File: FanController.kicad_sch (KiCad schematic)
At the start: 28 parts, among them J1 Conn_01x02_Female, J2 Conn_01x03_Male, J3 Conn_01x03_Male, J4 Conn_01x03_Male, J5 Conn_01x03_Male, Q1 AO3400A, Q2 AO3400A, Q3 AO3400A, Q4 AO3400A, U1 D-SUN-MP1584EN, U2 mh-et-live-minikit

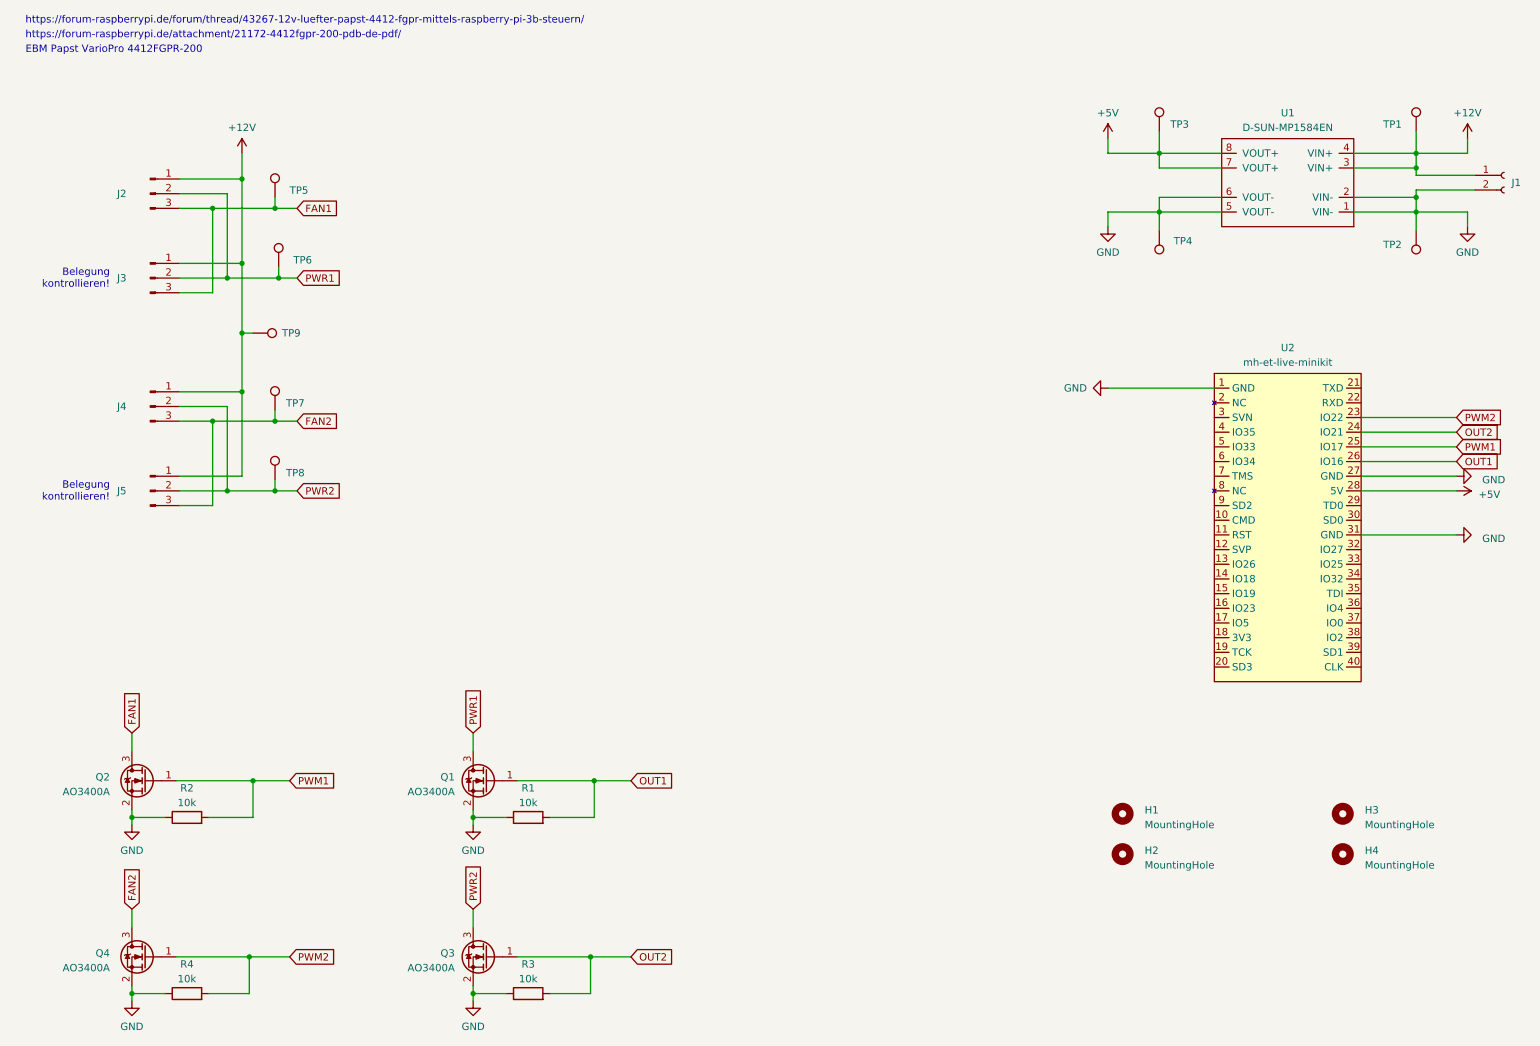
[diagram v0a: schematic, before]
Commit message: shrinked board
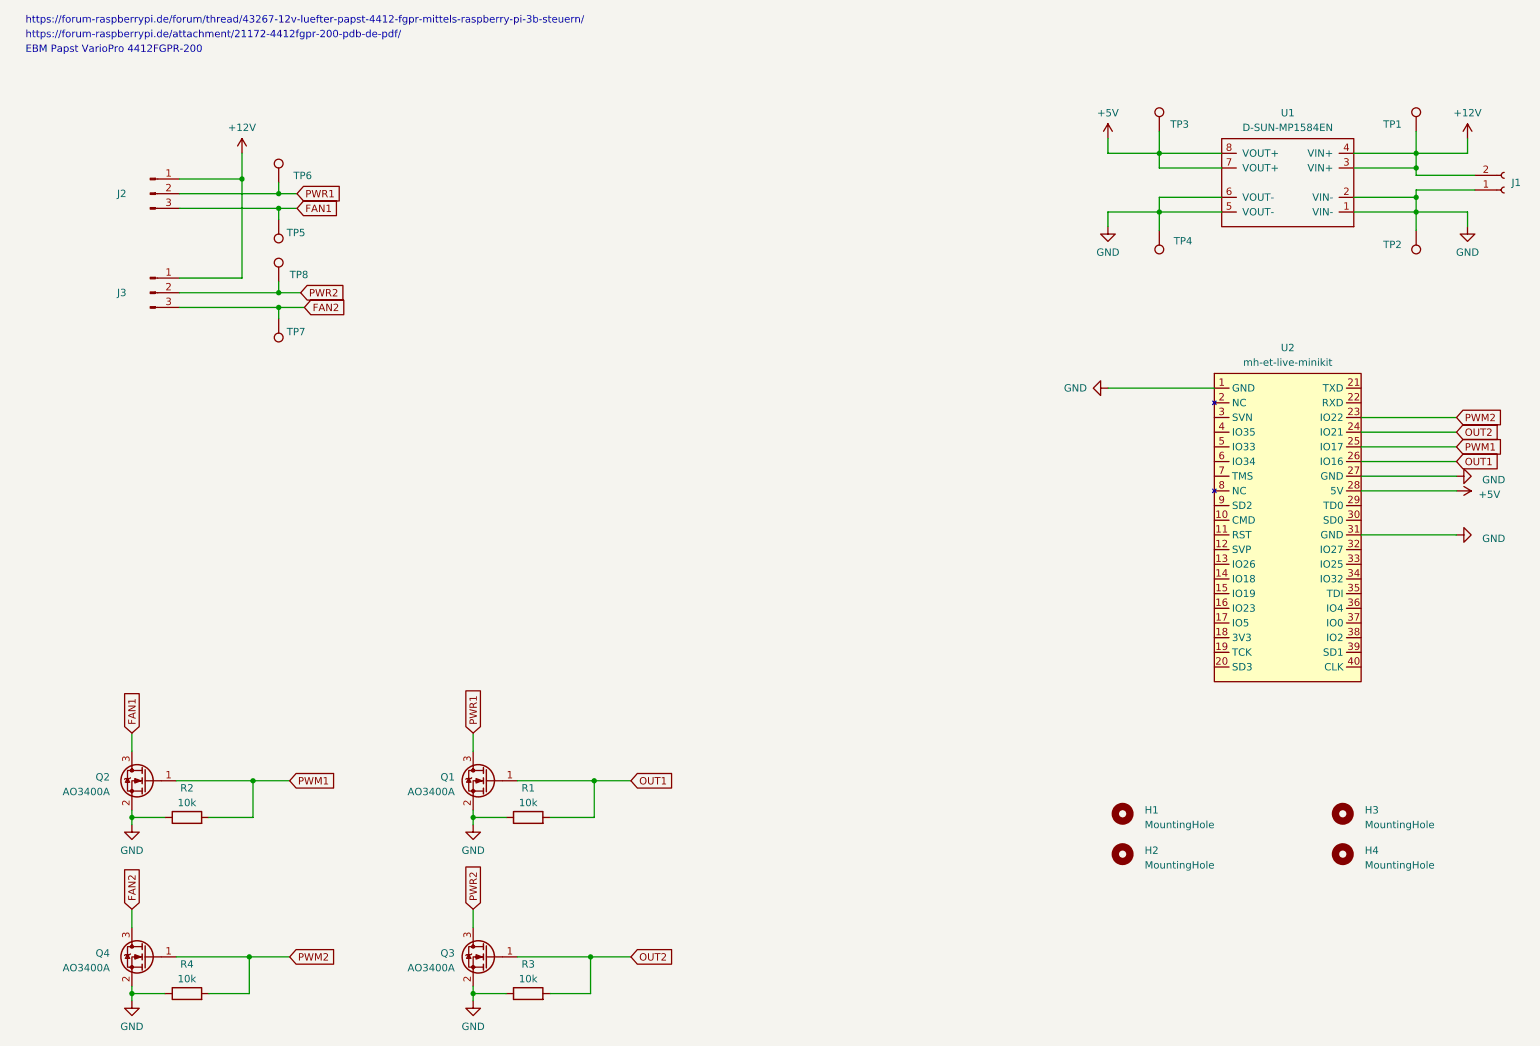
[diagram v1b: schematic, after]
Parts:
- removed J3, J5: Conn_01x03_Male, Connector_Molex:Molex_KK-254_AE-6410-03A_1x03_P2.54mm_Vertical, symbol Connector:Conn_01x03_Male
- removed TP9: TestPoint, TestPoint:TestPoint_Pad_D2.0mm, symbol Connector:TestPoint
- renumbered J4 to J3
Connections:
- net +12V: now also J1.2 (Pin_2); no longer J1.1 (Pin_1)
- net GND: now also J1.1 (Pin_1); no longer J1.2 (Pin_2)
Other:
- note removed: "Belegung kontrollieren!"
- moved on the sheet: J3, TP5, TP6, TP7, TP8
